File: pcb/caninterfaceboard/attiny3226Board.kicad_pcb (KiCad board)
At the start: 2 copper layers, 97 x 54.3 mm, 88 parts, among them J10 NTC2, J11 Attiny UDPI, J12 Flywheel, J13 1Wire, J2 CAN, J4 NTC3, J5 12V In, J6 FuelLevel, J7 Engine, J8 NTC1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

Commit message: Finally mare the RPM to pulse amp stable
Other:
- board text added: "0v"
- board text added: "Alt B+"
- board text added: "Alternator Temp"
- board text added: "CanH"
- board text added: "CanL"
- board text added: "Coolant"
- board text added: "Engine Block 0v"
- board text added: "Engine Room"
- board text added: "Engine Switched 12V"
- board text added: "Exhaust Temp"
- board text added: "Flywheel +"
- board text added: "Flywheel -"
- board text added: "Fuel Level"
- board text added: "Oil Pressure 0V"
- board text added: "Oil Pressure 5V"
- board text added: "Oil Pressure Signal"
- board text added: "OneWire 0v"
- board text added: "OneWire 5v"
- board text added: "OneWire Sig"
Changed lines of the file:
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@@
         (effects (font (size 1 1) (thickness 0.15)))
     )
-    (fp_text value "Flywheel" (at 2.54 5.66) (layer "F.Fab")
+    (fp_text value "Flywheel" (at 2.032 -10.668) (layer "F.Fab")
         (effects (font (size 1 1) (thickness 0.15)))
     )
@@
         (effects (font (size 1 1) (thickness 0.15)))
     )
-    (fp_text value "NTC3" (at 2.54 4.41) (layer "F.Fab")
+    (fp_text value "NTC3" (at 1.9812 -10.5158) (layer "F.Fab")
         (effects (font (size 1 1) (thickness 0.15)))
     )
@@
         (effects (font (size 1 1) (thickness 0.15)))
     )
-    (fp_text value "NTC1" (at 13.823 7.6412) (layer "F.Fab")
+    (fp_text value "NTC1" (at 1.9812 -10.414) (layer "F.Fab")
         (effects (font (size 1 1) (thickness 0.15)))
     )
@@
         (effects (font (size 1 1) (thickness 0.15)))
     )
-    (fp_text value "FuelLevel" (at 2.54 5.66) (layer "F.Fab")
+    (fp_text value "FuelLevel" (at 1.3258 -10.5666) (layer "F.Fab")
         (effects (font (size 1 1) (thickness 0.15)))
     )
@@
         (effects (font (size 1 1) (thickness 0.15)))
     )
-    (fp_text value "Engine" (at 2.54 5.66) (layer "F.Fab")
+    (fp_text value "Engine" (at 1.6256 -10.414) (layer "F.Fab")
         (effects (font (size 1 1) (thickness 0.15)))
     )
@@
         (effects (font (size 1 1) (thickness 0.15)))
     )
-    (fp_text value "Oil Pressure" (at 5.08 5.66) (layer "F.Fab")
+    (fp_text value "Oil Pressure" (at 4.5212 -10.7696) (layer "F.Fab")
         (effects (font (size 1 1) (thickness 0.15)))
     )
@@
         (effects (font (size 1 1) (thickness 0.15)))
     )
-    (fp_text value "NTC2" (at 2.54 5.66) (layer "F.Fab")
+    (fp_text value "NTC2" (at 2.3368 -10.5664) (layer "F.Fab")
         (effects (font (size 1 1) (thickness 0.15)))
     )
@@
     (effects (font (size 1.5 1.5) (thickness 0.3) bold) (justify left bottom))
   )
+  (gr_text "0v" (at 168.1988 44.5008 90) (layer "Dwgs.User")
+    (effects (font (size 1.5 1.5) (thickness 0.3) bold) (justify left bottom))
+  )
+  (gr_text "Engine Block 0v" (at 206.2988 98.044) (layer "Dwgs.User")
+    (effects (font (size 1.5 1.5) (thickness 0.3) bold) (justify left bottom))
+  )
+  (gr_text "Alt B+" (at 198.1708 45.1612 90) (layer "Dwgs.User")
+    (effects (font (size 1.5 1.5) (thickness 0.3) bold) (justify left bottom))
+  )
+  (gr_text "0v" (at 191.0588 44.5008 90) (layer "Dwgs.User")
+    (effects (font (size 1.5 1.5) (thickness 0.3) bold) (justify left bottom))
+  )
+  (gr_text "OneWire 0v" (at 95.8596 82.55) (layer "Dwgs.User")
+    (effects (font (size 1.5 1.5) (thickness 0.3) bold) (justify left bottom))
+  )
+  (gr_text "Engine Room" (at 152.4508 45.4152 90) (layer "Dwgs.User")
+    (effects (font (size 1.5 1.5) (thickness 0.3) bold) (justify left bottom))
+  )
+  (gr_text "0v" (at 157.0736 44.9072 90) (layer "Dwgs.User")
+    (effects (font (size 1.5 1.5) (thickness 0.3) bold) (justify left bottom))
+  )
+  (gr_text "Alternator Temp" (at 163.3728 46.4312 90) (layer "Dwgs.User")
+    (effects (font (size 1.5 1.5) (thickness 0.3) bold) (justify left bottom))
+  )
+  (gr_text "CanL" (at 205.9432 84.1248) (layer "Dwgs.User")
+    (effects (font (size 1.5 1.5) (thickness 0.3) bold) (justify left bottom))
+  )
+  (gr_text "Exhaust Temp" (at 174.8536 45.5168 90) (layer "Dwgs.User")
+    (effects (font (size 1.5 1.5) (thickness 0.3) bold) (justify left bottom))
+  )
+  (gr_text "OneWire 5v" (at 95.5548 87.7316) (layer "Dwgs.User")
+    (effects (font (size 1.5 1.5) (thickness 0.3) bold) (justify left bottom))
+  )
+  (gr_text "Oil Pressure 0V" (at 145.9484 44.704 90) (layer "Dwgs.User")
+    (effects (font (size 1.5 1.5) (thickness 0.3) bold) (justify left bottom))
+  )
+  (gr_text "Fuel Level" (at 186.4868 46.5328 90) (layer "Dwgs.User")
+    (effects (font (size 1.5 1.5) (thickness 0.3) bold) (justify left bottom))
+  )
+  (gr_text "Coolant" (at 202.692 45.6184 90) (layer "Dwgs.User")
+    (effects (font (size 1.5 1.5) (thickness 0.3) bold) (justify left bottom))
+  )
+  (gr_text "Oil Pressure Signal" (at 140.97 44.704 90) (layer "Dwgs.User")
+    (effects (font (size 1.5 1.5) (thickness 0.3) bold) (justify left bottom))
+  )
+  (gr_text "Oil Pressure 5V" (at 136.0932 44.8056 90) (layer "Dwgs.User")
+    (effects (font (size 1.5 1.5) (thickness 0.3) bold) (justify left bottom))
+  )
+  (gr_text "CanH" (at 206.4004 79.248) (layer "Dwgs.User")
+    (effects (font (size 1.5 1.5) (thickness 0.3) bold) (justify left bottom))
+  )
+  (gr_text "Engine Switched 12V" (at 206.2988 92.6084) (layer "Dwgs.User")
+    (effects (font (size 1.5 1.5) (thickness 0.3) bold) (justify left bottom))
+  )
+  (gr_text "Flywheel +" (at 127.8128 44.0944 90) (layer "Dwgs.User")
+    (effects (font (size 1.5 1.5) (thickness 0.3) bold) (justify left bottom))
+  )
+  (gr_text "OneWire Sig" (at 95.6056 92.5068) (layer "Dwgs.User")
+    (effects (font (size 1.5 1.5) (thickness 0.3) bold) (justify left bottom))
+  )
+  (gr_text "Flywheel -" (at 122.682 44.45 90) (layer "Dwgs.User")
+    (effects (font (size 1.5 1.5) (thickness 0.3) bold) (justify left bottom))
+  )
+  (gr_text "0v" (at 179.6288 44.6024 90) (layer "Dwgs.User")
+    (effects (font (size 1.5 1.5) (thickness 0.3) bold) (justify left bottom))
+  )
   (dimension (type aligned) (layer "Dwgs.User")
     (pts (xy 107.696 100.8888) (xy 107.696 97.2312))
@@
     (connect_pads yes (clearance 0.5))
     (min_thickness 0.5) (filled_areas_thickness no)
-    (fill yes (thermal_gap 0.5) (thermal_bridge_width 0.5) (smoothing fillet) (radius 1))
+    (fill (thermal_gap 0.5) (thermal_bridge_width 0.5) (smoothing fillet) (radius 1))
     (polygon
       (pts
@@
     (connect_pads yes (clearance 0.75))
     (min_thickness 0.75) (filled_areas_thickness no)
-    (fill yes (thermal_gap 0.75) (thermal_bridge_width 0.75) (smoothing fillet) (radius 1))
+    (fill (thermal_gap 0.75) (thermal_bridge_width 0.75) (smoothing fillet) (radius 1))
     (polygon
       (pts

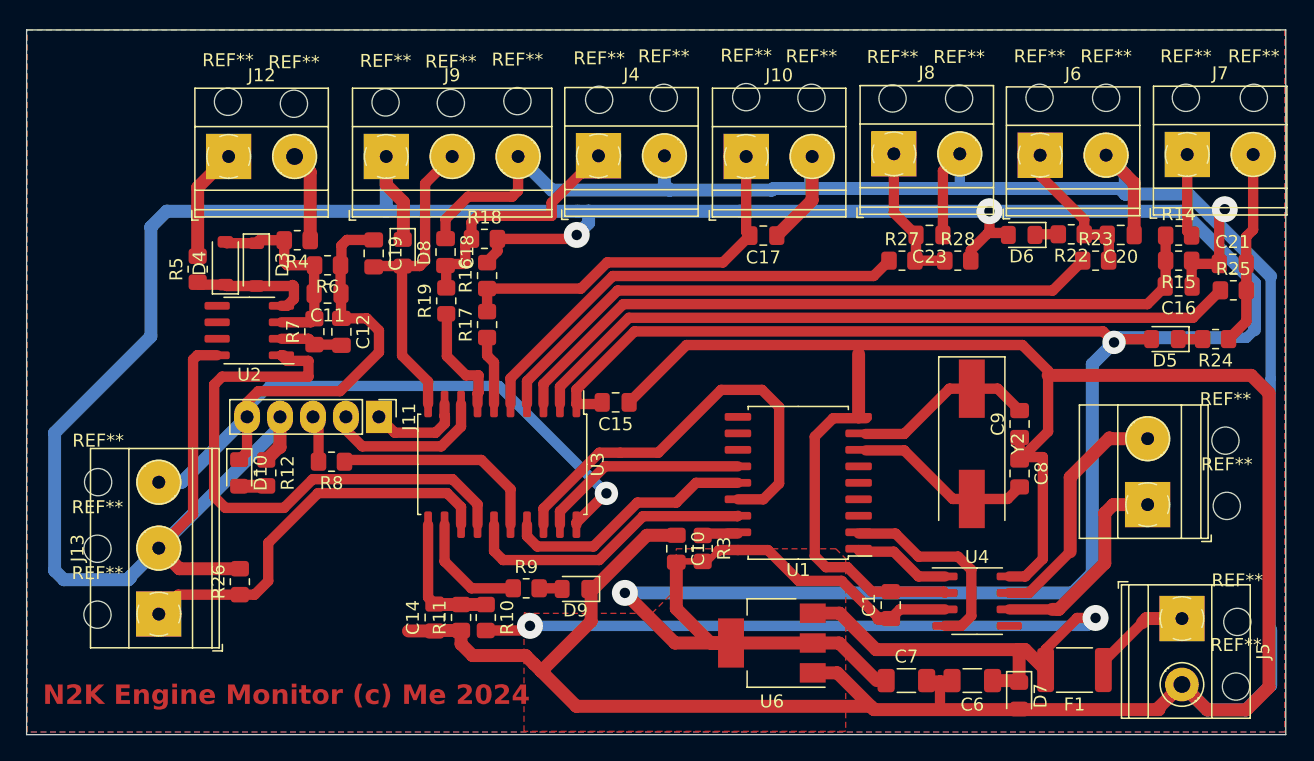
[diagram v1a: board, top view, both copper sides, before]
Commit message: Improved flywheel detection circuit
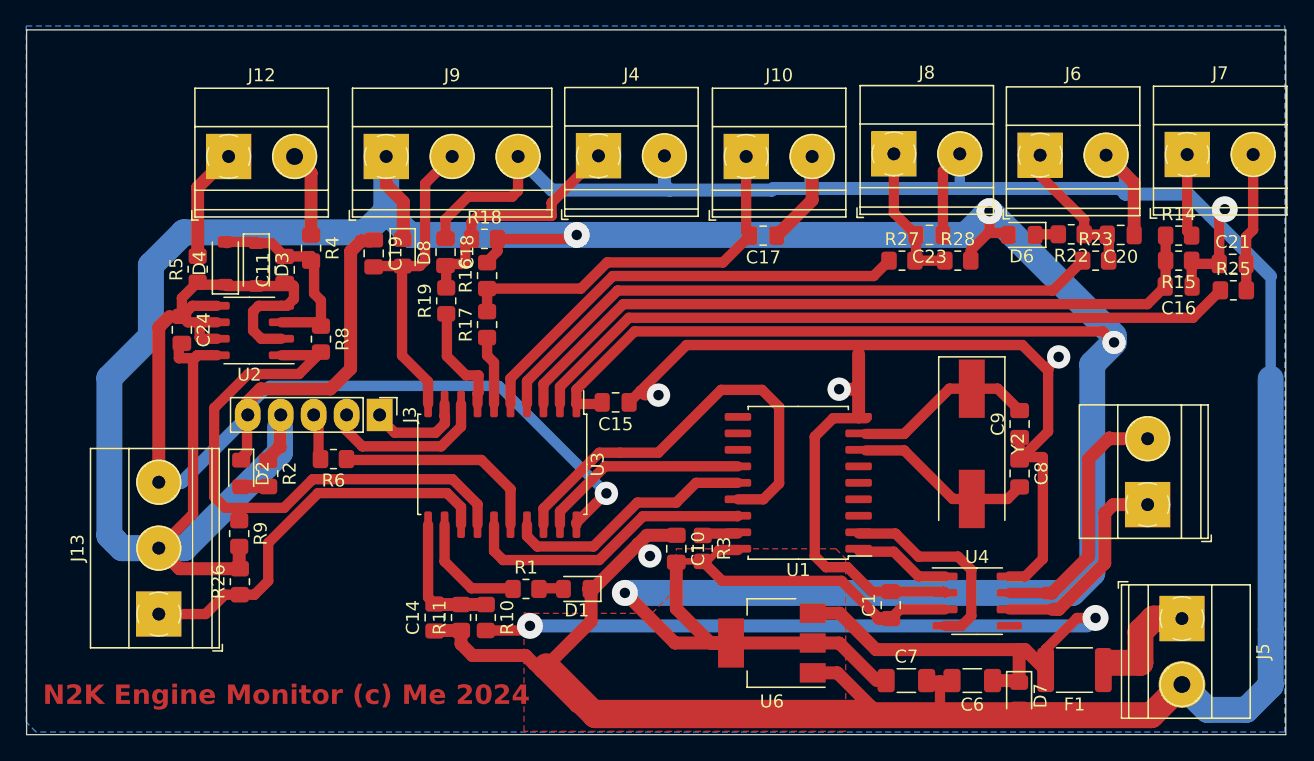
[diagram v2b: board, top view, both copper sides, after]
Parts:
- removed C12: 1uF, Capacitor_SMD:C_0805_2012Metric_Pad1.18x1.45mm_HandSolder
- removed D10, D9: LED, LED_SMD:LED_0805_2012Metric_Pad1.15x1.40mm_HandSolder
- removed D5: S1J, Diode_SMD:D_0805_2012Metric_Pad1.15x1.40mm_HandSolder
- removed J11: Attiny UDPI, Connector_PinHeader_2.54mm:PinHeader_1x05_P2.54mm_Vertical
- removed R12: 330R, Resistor_SMD:R_0805_2012Metric_Pad1.20x1.40mm_HandSolder
- removed R24: 1K, Resistor_SMD:R_0805_2012Metric_Pad1.20x1.40mm_HandSolder
- removed R7: 100K, Resistor_SMD:R_0805_2012Metric_Pad1.20x1.40mm_HandSolder
- removed REF** (x22): MountingHole_2.1mm, MountingHole:MountingHole_2.1mm
- added C24: 100nF, Capacitor_SMD:C_0805_2012Metric_Pad1.18x1.45mm_HandSolder, F.Cu at (119.6, 69.9)
- added D1: LED, LED_SMD:LED_0805_2012Metric_Pad1.15x1.40mm_HandSolder, F.Cu at (150.1, 89.9)
- added D2: LED, LED_SMD:LED_0805_2012Metric_Pad1.15x1.40mm_HandSolder, F.Cu at (124.2, 81.0)
- added J3: Attiny UDPI, Connector_PinHeader_2.54mm:PinHeader_1x05_P2.54mm_Vertical, F.Cu at (134.9, 76.5)
- added R1: 4K7, Resistor_SMD:R_0805_2012Metric_Pad1.20x1.40mm_HandSolder, F.Cu at (146.2, 89.9)
- added R2: 4K7, Resistor_SMD:R_0805_2012Metric_Pad1.20x1.40mm_HandSolder, F.Cu at (126.3, 81.0)
- C11: value 1uF -> 470nF
- D3, D4: value 1N5819 -> SJ1
- R10, R14: value 1M -> 100K
- R11, R15: value 470K -> 47K
- R17, R19, R23, R25, R27: value 100K -> 10K
- R6: value 1K -> 470R
- R8: value 1K -> 220K
- R9: value 330R -> 10K
- moved R9 22.5 mm to (124.1, 85.6), turned to -90 degrees
- moved R6 14.9 mm to (131.3, 79.9)
- moved R8 9.48 mm to (130.4, 70.6), turned to -90 degrees
- moved C11 3.77 mm to (127.6, 65.3), turned to 90 degrees
- moved R4 1.23 mm to (129.6, 63.6), turned to -90 degrees
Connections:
- net A0 renamed PA5
- net A1 renamed PA6
- net A2 renamed PA7
- net A3 renamed PB5
- net A4 renamed PB4
- net A5 renamed PB1
- net A6 renamed PA4
- net A7 renamed PB0
- net D10 renamed PC3
- net D3 renamed PC1
- R6 pad 1: Engine Block -> Net-(U3-~{RESET}/PA0)
- R6 pad 2: Net-(D3-K) -> UDPI
- R8 pad 1: Net-(U3-~{RESET}/PA0) -> Net-(D3-K)
- R8 pad 2: UDPI -> PC2
- R9 pad 1: IND -> PC2
- R9 pad 2: Net-(D9-A) -> 5V
- U2 pad 1: D2 -> PC2
- U2 pad 2: Net-(U2A--) -> Engine Block
- U2 pad 5: unconnected-(U2B-+-Pad5) -> Engine Block
- U2 pad 6: unconnected-(U2B---Pad6) -> Engine Block
- U2 pad 7: unconnected-(U2-Pad7) -> Engine Block
- U3 pad 12: IND -> PC0
- U3 pad 14: D2 -> PC2
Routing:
- net PC2: track 0.00 -> 44.8 mm
- net D2: track 43.8 -> 0.00 mm
- net 5V: track 371.5 -> 342.6 mm
- net Engine Block: track 466.4 -> 493.4 mm, vias 2 -> 6
- net PC0: track 0.00 -> 8.98 mm
- net IND: track 8.98 -> 0.00 mm
- net Net-(U2A--): track 4.83 -> 0.00 mm
- net Coolant: track 15.7 -> 11.4 mm
- net Net-(D10-A): track 2.09 -> 0.00 mm
- net Net-(D2-A): track 0.00 -> 2.09 mm
- net Net-(D5-K): track 1.88 -> 0.00 mm
- net Net-(D9-A): track 1.79 -> 0.00 mm
- net Net-(D1-A): track 0.00 -> 1.79 mm
- net 12V: track 8.07 -> 9.74 mm
- net CANH: track 19.0 -> 20.1 mm
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- removed copper zone on F.Cu, net Engine Block

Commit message: Added protection for ovre voltages on measurements
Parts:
- added D11: S1J, Diode_SMD:D_0805_2012Metric_Pad1.15x1.40mm_HandSolder, F.Cu at (142.0, 67.7)
- added D12: S1J, Diode_SMD:D_0805_2012Metric_Pad1.15x1.40mm_HandSolder, F.Cu at (126.2, 89.4)
- added D13: S1J, Diode_SMD:D_0805_2012Metric_Pad1.15x1.40mm_HandSolder, F.Cu at (144.0, 67.7)
- added D14: S1J, Diode_SMD:D_0805_2012Metric_Pad1.15x1.40mm_HandSolder, F.Cu at (172.8, 62.6)
- added D15: S1J, Diode_SMD:D_0805_2012Metric_Pad1.15x1.40mm_HandSolder, F.Cu at (184.3, 64.9)
- added D5: S1J, Diode_SMD:D_0805_2012Metric_Pad1.15x1.40mm_HandSolder, F.Cu at (200.7, 68.9)
- added R7: 10K, Resistor_SMD:R_0805_2012Metric_Pad1.20x1.40mm_HandSolder, F.Cu at (135.2, 63.7)
- moved R17 3.46 mm to (146.2, 67.8)
- moved C19 3.46 mm to (137.9, 63.9)
- moved D8 3.36 mm to (133.3, 63.7)
- moved R16 2.13 mm to (145.1, 64.8), turned to 180 degrees
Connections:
- C19 pad 2: PB1 -> Net-(J9-Pin_2)
- J9 pad 2: PB1 -> Net-(J9-Pin_2)
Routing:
- net 5V: track 342.6 -> 364.9 mm, vias 4 -> 5
- net Engine Block: track 493.4 -> 472.0 mm
- net Net-(J9-Pin_2): track 0.00 -> 14.4 mm
- net PB1: track 24.5 -> 14.3 mm
- net PB5: track 5.34 -> 10.0 mm
- net PA6: track 48.4 -> 52.3 mm
- net Net-(J10-Pin_1): track 30.7 -> 27.2 mm
- net PA7: track 34.9 -> 37.1 mm
- net PA4: track 55.3 -> 56.4 mm
- net PB4: track 8.58 -> 9.23 mm

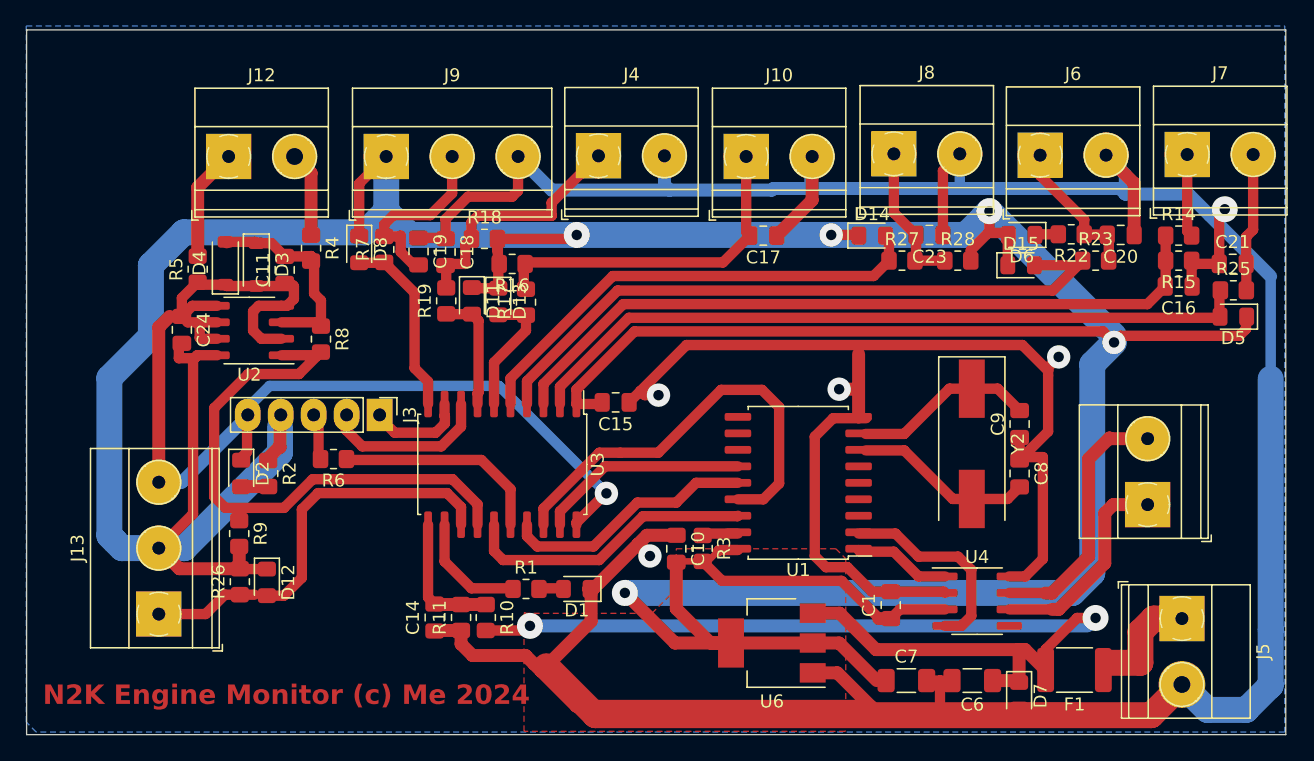
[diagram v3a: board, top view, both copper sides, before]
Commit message: Improvd ADC stability
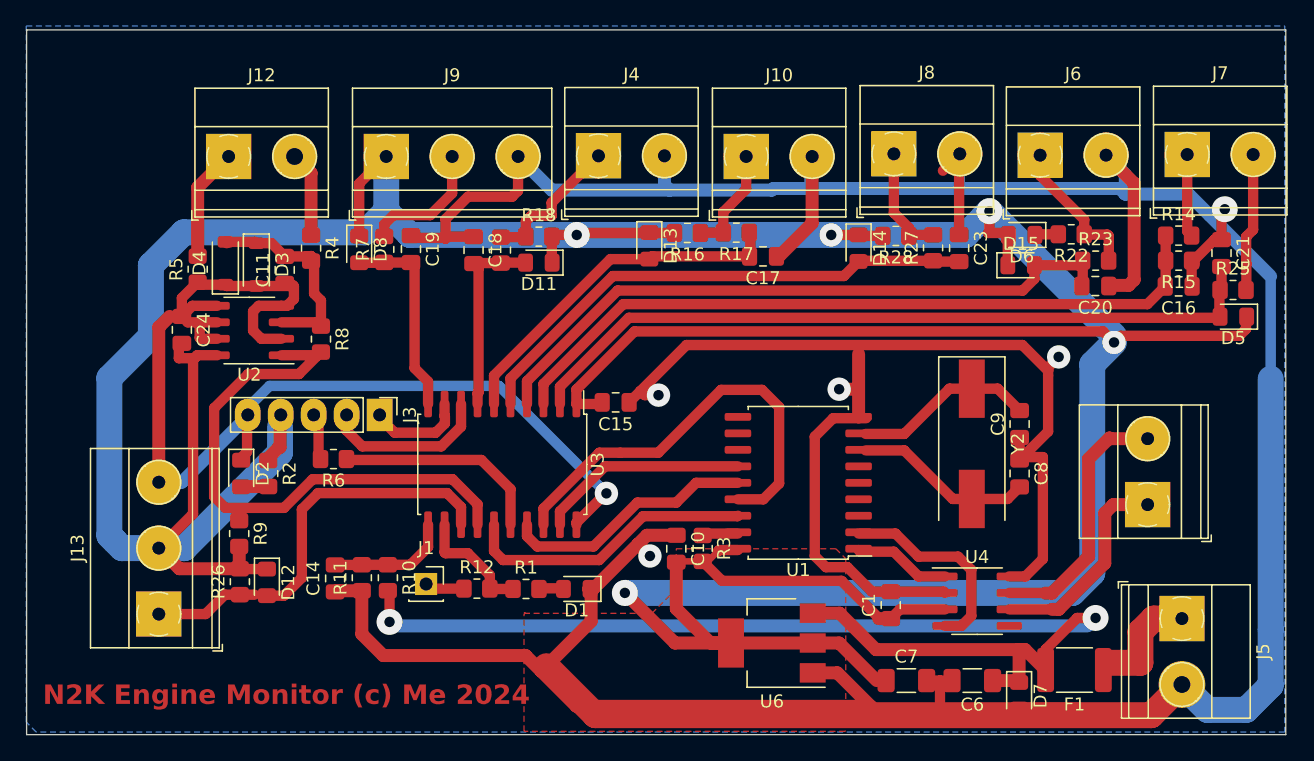
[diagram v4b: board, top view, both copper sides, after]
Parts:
- added J1: StopSolenoid, Connector_PinSocket_2.54mm:PinSocket_1x01_P2.54mm_Vertical, F.Cu at (138.5, 89.5)
- added R12: 10K, Resistor_SMD:R_0805_2012Metric_Pad1.20x1.40mm_HandSolder, F.Cu at (142.4, 89.8)
- C14, C16: value 1nF -> 470nF
- C21: value 10nF -> 10uF
- moved R17 17.1 mm to (162.4, 62.4), turned to 180 degrees
- moved R16 13.7 mm to (158.6, 62.4)
- moved D13 12.4 mm to (155.7, 63.4)
- moved C14 8.24 mm to (131.4, 89.1)
- moved R11 8.24 mm to (133.5, 89.0)
- moved R10 8.14 mm to (135.5, 89.0)
- moved D11 5.94 mm to (147.1, 64.7), turned to 180 degrees
- moved R19 5.75 mm to (144.2, 63.8)
- moved R28 5.14 mm to (174.7, 62.7), turned to 180 degrees
- moved C20 4.40 mm to (190.0, 66.5)
- moved R18 4.19 mm to (147.1, 62.7)
- moved R27 2.59 mm to (177.5, 63.6), turned to 90 degrees
- moved C23 2.50 mm to (179.5, 63.6), turned to -90 degrees
- moved C18 2.16 mm to (142.1, 63.8)
- moved C17 1.60 mm to (164.4, 64.2)
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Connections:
- C17 pad 2: Net-(J10-Pin_1) -> PB5
- C18 pad 2: Net-(J4-Pin_1) -> PB4
- C19 pad 2: Net-(J9-Pin_2) -> PB1
- C20 pad 2: Net-(J6-Pin_1) -> PA6
- C21 pad 2: Coolant -> PA4
- C23 pad 2: Net-(J8-Pin_1) -> PA7
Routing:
- net Engine Block: track 472.0 -> 492.8 mm
- net Net-(J10-Pin_1): track 27.2 -> 8.62 mm
- net PB5: track 10.0 -> 27.7 mm
- net Engine Batt+: track 77.8 -> 87.6 mm
- net Net-(J4-Pin_1): track 19.2 -> 11.4 mm
- net PB4: track 9.23 -> 15.0 mm
- net Net-(J9-Pin_2): track 14.4 -> 9.99 mm
- net PA7: track 37.1 -> 40.3 mm
- net Net-(J1-Pin_1): track 0.00 -> 3.06 mm
- net Net-(J8-Pin_1): track 11.3 -> 8.71 mm
- net PA4: track 56.4 -> 58.2 mm
- net 5V: track 364.9 -> 363.1 mm
- net PA6: track 52.3 -> 51.0 mm
- net PB1: track 14.3 -> 15.5 mm
- net PB0: track 10.3 -> 9.46 mm
